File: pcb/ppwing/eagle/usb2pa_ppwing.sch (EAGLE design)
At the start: 50 parts, among them Q1 24 MHz, SW1 EVQQ2, U2 LM3525-H, U3 INA219AID

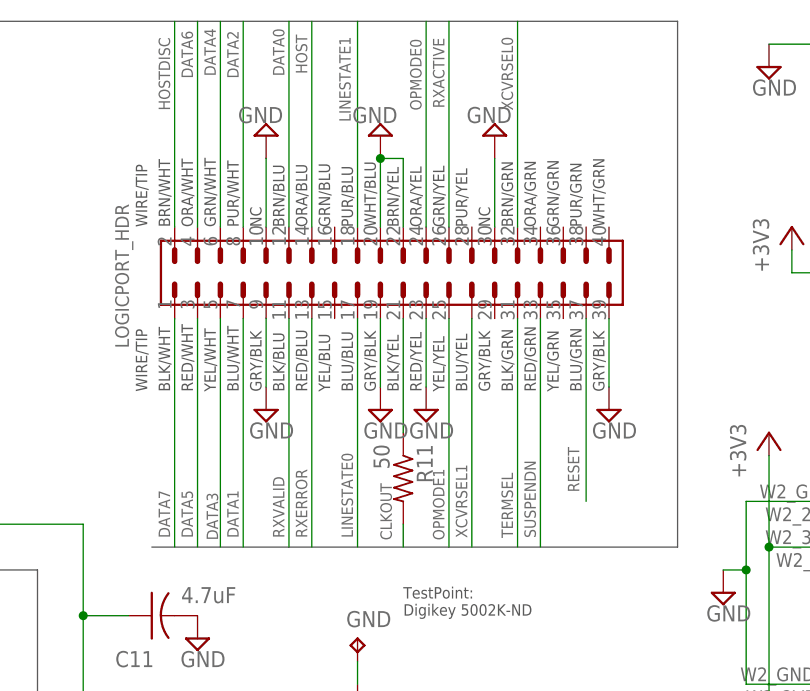
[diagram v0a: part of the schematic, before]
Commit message: REV0P1a : This is what was actually submitted to the board shop.
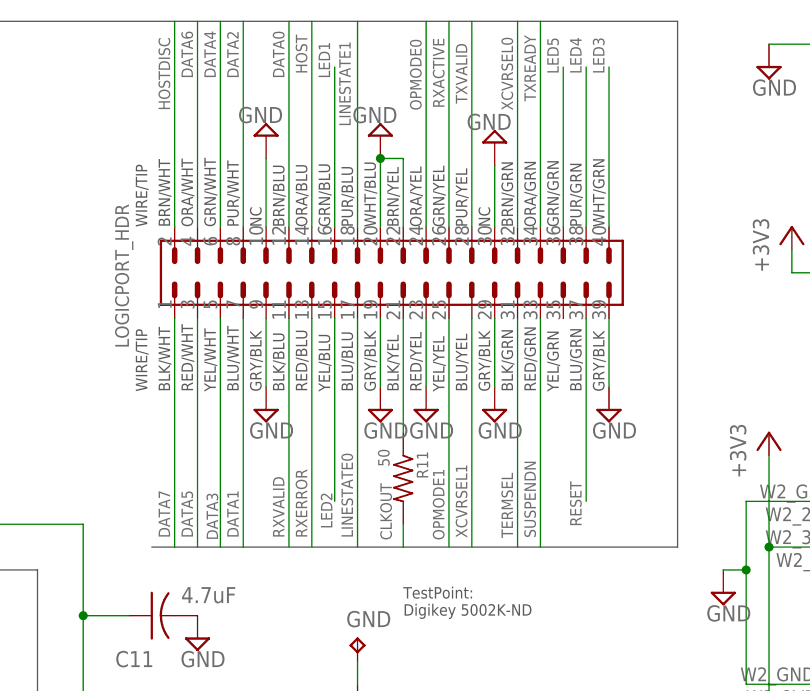
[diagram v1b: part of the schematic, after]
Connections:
- net GND: now also LOGICPORT_HDR.29
- net LED1: now also LOGICPORT_HDR.16
- net LED2: now also LOGICPORT_HDR.15
- net LED3: now also LOGICPORT_HDR.40
- net LED4: now also LOGICPORT_HDR.38
- net LED5: now also LOGICPORT_HDR.36
- net TXREADY: now also LOGICPORT_HDR.34
- net TXVALID: now also LOGICPORT_HDR.28
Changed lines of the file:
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@@
 <part name="SUPPLY30" library="supply2" deviceset="GND" device=""/>
 <part name="CC_LICENSE" library="Cory" deviceset="CC_LICENSE" device=""/>
+<part name="SUPPLY31" library="supply2" deviceset="GND" device=""/>
 </parts>
 <sheets>
@@
 <attribute name="VALUE" x="104.14" y="22.225" size="1.27" layer="96" rot="MR0"/>
 </instance>
-<instance part="R11" gate="G$1" x="170.18" y="121.92" rot="R270"/>
+<instance part="R11" gate="G$1" x="170.18" y="121.92" smashed="yes" rot="R270">
+<attribute name="NAME" x="171.6786" y="124.968" size="1.27" layer="95" rot="R270"/>
+<attribute name="VALUE" x="167.386" y="125.222" size="1.27" layer="96" rot="R270"/>
+</instance>
 <instance part="SUPPLY19" gate="GND" x="154.94" y="129.54"/>
 <instance part="SUPPLY20" gate="GND" x="167.64" y="129.54"/>
 <instance part="SUPPLY21" gate="GND" x="172.72" y="129.54"/>
 <instance part="SUPPLY22" gate="GND" x="193.04" y="129.54"/>
-<instance part="SUPPLY23" gate="GND" x="180.34" y="160.02" rot="R180"/>
+<instance part="SUPPLY23" gate="GND" x="180.34" y="159.258" rot="R180"/>
 <instance part="SUPPLY24" gate="GND" x="154.94" y="160.02" rot="R180"/>
 <instance part="SUPPLY25" gate="GND" x="167.64" y="160.02" rot="R180"/>
@@
 <instance part="SUPPLY30" gate="GND" x="160.02" y="55.88"/>
 <instance part="CC_LICENSE" gate="G$1" x="165.1" y="25.4"/>
+<instance part="SUPPLY31" gate="GND" x="180.34" y="129.54"/>
 </instances>
 <busses>
@@
 <pinref part="SUPPLY23" gate="GND" pin="GND"/>
 <pinref part="LOGICPORT_HDR" gate="G$1" pin="30"/>
-<wire x1="180.34" y1="157.48" x2="180.34" y2="149.86" width="0.1524" layer="91"/>
+<wire x1="180.34" y1="156.718" x2="180.34" y2="149.86" width="0.1524" layer="91"/>
 </segment>
 <segment>
@@
 <wire x1="162.56" y1="66.04" x2="160.02" y2="66.04" width="0.1524" layer="91"/>
 <junction x="160.02" y="66.04"/>
+</segment>
+<segment>
+<pinref part="SUPPLY31" gate="GND" pin="GND"/>
+<pinref part="LOGICPORT_HDR" gate="G$1" pin="29"/>
+<wire x1="180.34" y1="132.08" x2="180.34" y2="139.7" width="0.1524" layer="91"/>
 </segment>
 </net>
@@
 <pinref part="LOGICPORT_HDR" gate="G$1" pin="37"/>
 <wire x1="190.5" y1="139.7" x2="190.5" y2="119.38" width="0.1524" layer="91"/>
-<label x="189.738" y="120.396" size="1.27" layer="95" rot="R90"/>
+<label x="189.992" y="116.586" size="1.27" layer="95" rot="R90"/>
 </segment>
 </net>
@@
 <label x="16.51" y="99.314" size="1.27" layer="95"/>
 </segment>
+<segment>
+<pinref part="LOGICPORT_HDR" gate="G$1" pin="16"/>
+<wire x1="162.56" y1="149.86" x2="162.56" y2="167.64" width="0.1524" layer="91"/>
+<label x="162.052" y="166.37" size="1.27" layer="95" rot="R90"/>
+</segment>
 </net>
 <net name="LED2" class="0">
@@
 <label x="16.51" y="101.854" size="1.27" layer="95"/>
 </segment>
+<segment>
+<pinref part="LOGICPORT_HDR" gate="G$1" pin="15"/>
+<wire x1="162.56" y1="139.7" x2="162.56" y2="119.38" width="0.1524" layer="91"/>
+<label x="162.306" y="116.332" size="1.27" layer="95" rot="R90"/>
+</segment>
 </net>
 <net name="LED3" class="0">
@@
 <label x="43.434" y="102.108" size="1.27" layer="95"/>
 </segment>
+<segment>
+<pinref part="LOGICPORT_HDR" gate="G$1" pin="40"/>
+<wire x1="193.04" y1="149.86" x2="193.04" y2="167.64" width="0.1524" layer="91"/>
+<label x="192.532" y="166.878" size="1.27" layer="95" rot="R90"/>
+</segment>
 </net>
 <net name="LED4" class="0">
@@
 <label x="43.434" y="99.314" size="1.27" layer="95"/>
 </segment>
+<segment>
+<pinref part="LOGICPORT_HDR" gate="G$1" pin="38"/>
+<wire x1="190.5" y1="149.86" x2="190.5" y2="167.64" width="0.1524" layer="91"/>
+<label x="189.992" y="166.878" size="1.27" layer="95" rot="R90"/>
+</segment>
 </net>
 <net name="LED5" class="0">
@@
 <label x="43.434" y="96.774" size="1.27" layer="95"/>
 </segment>
+<segment>
+<pinref part="LOGICPORT_HDR" gate="G$1" pin="36"/>
+<wire x1="187.96" y1="149.86" x2="187.96" y2="167.64" width="0.1524" layer="91"/>
+<label x="187.452" y="166.878" size="1.27" layer="95" rot="R90"/>
+</segment>
 </net>
 <net name="N$3" class="0">
@@
 <pinref part="LOGICPORT_HDR" gate="G$1" pin="18"/>
 <wire x1="165.1" y1="149.86" x2="165.1" y2="172.72" width="0.1524" layer="91"/>
-<label x="164.338" y="161.544" size="1.27" layer="95" rot="R90"/>
+<label x="164.338" y="161.036" size="1.27" layer="95" rot="R90"/>
 </segment>
 </net>
@@
 <pinref part="LOGICPORT_HDR" gate="G$1" pin="6"/>
 <wire x1="149.86" y1="149.86" x2="149.86" y2="172.72" width="0.1524" layer="91"/>
-<label x="149.352" y="166.624" size="1.27" layer="95" rot="R90"/>
+<label x="149.352" y="166.37" size="1.27" layer="95" rot="R90"/>
 </segment>
 </net>
@@
 <pinref part="LOGICPORT_HDR" gate="G$1" pin="12"/>
 <wire x1="157.48" y1="149.86" x2="157.48" y2="172.72" width="0.1524" layer="91"/>
-<label x="156.972" y="166.624" size="1.27" layer="95" rot="R90"/>
+<label x="156.972" y="166.37" size="1.27" layer="95" rot="R90"/>
 </segment>
 </net>
@@
 <label x="8.89" y="71.374" size="1.27" layer="95"/>
 </segment>
+<segment>
+<pinref part="LOGICPORT_HDR" gate="G$1" pin="34"/>
+<wire x1="185.42" y1="149.86" x2="185.42" y2="172.72" width="0.1524" layer="91"/>
+<label x="184.912" y="163.83" size="1.27" layer="95" rot="R90"/>
+</segment>
 </net>
 <net name="SUSPENDN" class="0">
@@
 <label x="8.89" y="74.168" size="1.27" layer="95"/>
 </segment>
-</net>
+<segment>
+<pinref part="LOGICPORT_HDR" gate="G$1" pin="28"/>
+<wire x1="177.8" y1="149.86" x2="177.8" y2="172.72" width="0.1524" layer="91"/>
+<label x="177.292" y="163.576" size="1.27" layer="95" rot="R90"/>
+</segment>
+</net>
